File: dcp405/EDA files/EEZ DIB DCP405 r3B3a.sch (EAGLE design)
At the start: 317 parts, among them IC1 LM5145RGYT, IC10 TL072D, IC11 LTC2050HVCS8#PBF, IC12 SN74LVC1G3157DCKR, IC13 74AUP1G74DC.125, IC14 MCP23S17-E/SS, IC15 REF5025AIDR, IC16 TC77-5.0MCTTR, IC17 DAC8552IDGKR, IC18 SN74LVC1G3157DCKR, IC19 ADS1120IPWR, IC2 TPS54060DGQ, IC20 LM293D, IC21 MAX9141ESA, IC3 SI8641BB-B-IS1, IC4 SN74LVC1G139DCUR, IC5 MC78L05, IC6 MC79L05, IC7 SI8641BB-B-IS1, IC8 M24C32-WMN6P, IC9 TL072D, J1 4907, J2 FCR7350R, J3 FCR7350B, K1 FTR-C1GA005G-B05, Q1 BSC117N08NS5ATMA1, Q10 2N7002, Q11 BSS205NH6327XTSA1, Q12 PSMN0R9-25YLC, Q13 PSMN0R9-25YLC, Q14 BSS84P, Q15 BT139B-600E, Q16 2N7002, Q17 FMMT493TA, Q18 2N7002, Q19 PSMN013-60YL, Q2 BSC039N06NSATMA1, Q20 MMBT5551, Q21 2N7002, Q22 MMBT5401, Q23 MMBT5551, Q24 MMBT5551, Q25 2N7002, Q3 MMBT5401, Q4 D45H11FP, Q5 D45H11FP, Q6 FQPF11P06 or FQPF27P06, Q7 BCP56-16.115, Q8 MMBT5401, Q9 NZT605, X1 39-30-1020, X2 77317-104-20LF, X3 691322110005, X4 DS1024-2*10R0

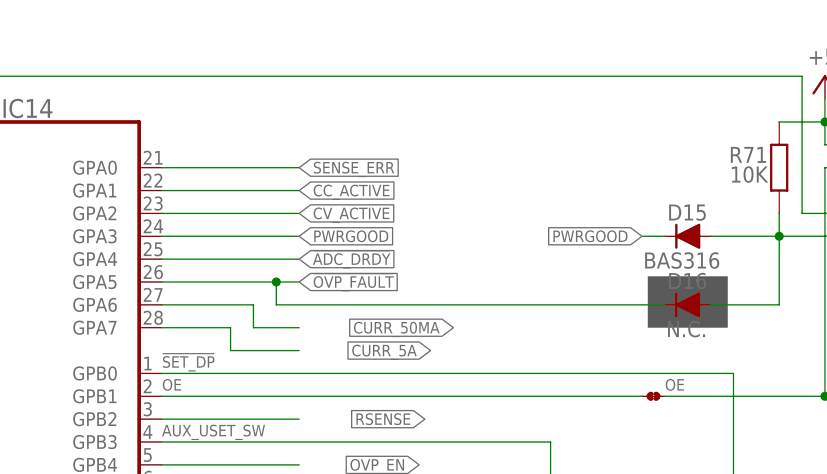
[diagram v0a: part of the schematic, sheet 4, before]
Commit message: Update Note 3.1. in DCP405 schematics
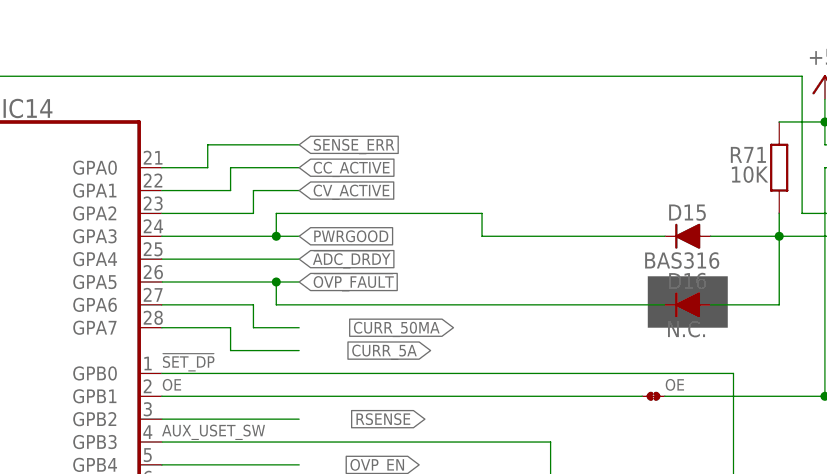
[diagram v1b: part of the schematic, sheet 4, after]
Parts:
- K1: device EEZ_Lib1:FTR-C1 -> EEZ_switches:FTR-C1
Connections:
- net N$115: now also K1-1.NO; no longer K1-1.O
- net N$116: now also K1-2.NO; no longer K1-2.O
- net POST_OUT+: now also K1-1.NC; no longer K1-1.S
- net POST_OUT-: now also K1-2.NC; no longer K1-2.S
- net SENSE+: now also K1-1.COM; no longer K1-1.P
- net SENSE-: now also K1-2.COM; no longer K1-2.P
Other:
- note added: "Note 3.1: Q4, Q5 and Q6 mounted on heatsink KK3"
- note removed: "Note 3.1: Q5, Q6 and Q7 mounted on heatsink KK3"
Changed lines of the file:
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@@
 <part name="C60" library="rcl" deviceset="C-EU" device="C0603" value="100n"/>
 <part name="P+14" library="supply2" deviceset="V+" device=""/>
-<part name="K1" library="EEZ_Lib1" deviceset="FTR-C1" device="" value="FTR-C1GA005G-B05"/>
+<part name="K1" library="EEZ_switches" deviceset="FTR-C1" device="" value="FTR-C1GA005G-B05"/>
 <part name="R3" library="rcl" deviceset="R-EU_" device="R0805" value="10K"/>
 <part name="D1" library="EEZ_Lib1" deviceset="DIODE" device="SOD323R" value="BAS316"/>
@@
 <wire x1="99.06" y1="119.38" x2="99.06" y2="73.66" width="0.1524" layer="97" style="shortdash"/>
 <wire x1="99.06" y1="73.66" x2="99.06" y2="58.42" width="0.1524" layer="97" style="shortdash"/>
-<text x="5.08" y="15.24" size="1.4224" layer="103">Note 3.1: Q5, Q6 and Q7 mounted on heatsink KK3</text>
+<text x="5.08" y="15.24" size="1.4224" layer="103">Note 3.1: Q4, Q5 and Q6 mounted on heatsink KK3</text>
 <wire x1="106.68" y1="173.99" x2="180.34" y2="173.99" width="0.1524" layer="97" style="shortdash"/>
 <wire x1="73.66" y1="58.42" x2="73.66" y2="17.78" width="0.1524" layer="97" style="shortdash"/>
@@
 <label x="86.36" y="154.94" size="1.27" layer="102" xref="yes"/>
 <pinref part="IC14" gate="A" pin="GPA3"/>
-<wire x1="71.12" y1="154.94" x2="86.36" y2="154.94" width="0.1524" layer="91"/>
-</segment>
-<segment>
+<wire x1="71.12" y1="154.94" x2="83.82" y2="154.94" width="0.1524" layer="91"/>
+<wire x1="83.82" y1="154.94" x2="86.36" y2="154.94" width="0.1524" layer="91"/>
+<wire x1="83.82" y1="154.94" x2="83.82" y2="157.48" width="0.1524" layer="91"/>
+<junction x="83.82" y="154.94"/>
 <pinref part="D15" gate="G$1" pin="C"/>
-<wire x1="127" y1="154.94" x2="124.46" y2="154.94" width="0.1524" layer="91"/>
-<label x="124.46" y="154.94" size="1.27" layer="102" rot="R180" xref="yes"/>
+<wire x1="127" y1="154.94" x2="106.68" y2="154.94" width="0.1524" layer="91"/>
+<wire x1="83.82" y1="157.48" x2="106.68" y2="157.48" width="0.1524" layer="91"/>
+<wire x1="106.68" y1="157.48" x2="106.68" y2="154.94" width="0.1524" layer="91"/>
 </segment>
 </net>
@@
 <net name="CV_ACTIVE" class="0">
 <segment>
-<label x="86.36" y="157.48" size="1.27" layer="102" xref="yes"/>
+<label x="86.36" y="160.02" size="1.27" layer="102" xref="yes"/>
 <pinref part="IC14" gate="A" pin="GPA2"/>
-<wire x1="71.12" y1="157.48" x2="86.36" y2="157.48" width="0.1524" layer="91"/>
+<wire x1="86.36" y1="160.02" x2="81.28" y2="160.02" width="0.1524" layer="91"/>
+<wire x1="81.28" y1="160.02" x2="81.28" y2="157.48" width="0.1524" layer="91"/>
+<wire x1="81.28" y1="157.48" x2="71.12" y2="157.48" width="0.1524" layer="91"/>
 </segment>
 </net>
 <net name="CC_ACTIVE" class="0">
 <segment>
-<label x="86.36" y="160.02" size="1.27" layer="102" xref="yes"/>
+<label x="86.36" y="162.56" size="1.27" layer="102" xref="yes"/>
 <pinref part="IC14" gate="A" pin="GPA1"/>
-<wire x1="71.12" y1="160.02" x2="86.36" y2="160.02" width="0.1524" layer="91"/>
+<wire x1="71.12" y1="160.02" x2="78.74" y2="160.02" width="0.1524" layer="91"/>
+<wire x1="78.74" y1="160.02" x2="78.74" y2="162.56" width="0.1524" layer="91"/>
+<wire x1="78.74" y1="162.56" x2="86.36" y2="162.56" width="0.1524" layer="91"/>
 </segment>
 </net>
@@
 <net name="SENSE_ERR" class="0">
 <segment>
-<label x="86.36" y="162.56" size="1.27" layer="102" xref="yes"/>
+<label x="86.36" y="165.1" size="1.27" layer="102" xref="yes"/>
 <pinref part="IC14" gate="A" pin="GPA0"/>
-<wire x1="71.12" y1="162.56" x2="86.36" y2="162.56" width="0.1524" layer="91"/>
+<wire x1="71.12" y1="162.56" x2="76.2" y2="162.56" width="0.1524" layer="91"/>
+<wire x1="76.2" y1="162.56" x2="76.2" y2="165.1" width="0.1524" layer="91"/>
+<wire x1="76.2" y1="165.1" x2="86.36" y2="165.1" width="0.1524" layer="91"/>
 </segment>
 </net>
@@
 <wire x1="162.56" y1="170.18" x2="152.4" y2="170.18" width="0.4064" layer="91"/>
 <label x="162.56" y="170.18" size="1.27" layer="102" rot="MR180" xref="yes"/>
-<pinref part="K1" gate="-1" pin="S"/>
+<pinref part="K1" gate="-1" pin="NC"/>
 <wire x1="152.4" y1="170.18" x2="149.86" y2="170.18" width="0.4064" layer="91"/>
 <wire x1="111.76" y1="160.02" x2="114.3" y2="160.02" width="0.1524" layer="91"/>
@@
 <wire x1="96.52" y1="157.48" x2="96.52" y2="139.7" width="0.1524" layer="91"/>
 <junction x="96.52" y="139.7"/>
-<pinref part="K1" gate="-1" pin="P"/>
+<pinref part="K1" gate="-1" pin="COM"/>
 <wire x1="96.52" y1="157.48" x2="104.14" y2="157.48" width="0.1524" layer="91"/>
 </segment>
@@
 <junction x="96.52" y="124.46"/>
 <wire x1="71.12" y1="124.46" x2="96.52" y2="124.46" width="0.1524" layer="91"/>
-<pinref part="K1" gate="-2" pin="P"/>
+<pinref part="K1" gate="-2" pin="COM"/>
 <wire x1="104.14" y1="106.68" x2="96.52" y2="106.68" width="0.1524" layer="91"/>
 </segment>
@@
 <wire x1="114.3" y1="104.14" x2="114.3" y2="99.06" width="0.1524" layer="91"/>
 <junction x="114.3" y="99.06"/>
-<pinref part="K1" gate="-2" pin="S"/>
+<pinref part="K1" gate="-2" pin="NC"/>
 <wire x1="111.76" y1="104.14" x2="114.3" y2="104.14" width="0.1524" layer="91"/>
 <wire x1="162.56" y1="119.38" x2="157.48" y2="119.38" width="0.4064" layer="91"/>
@@
 <wire x1="203.2" y1="152.4" x2="114.3" y2="152.4" width="0.1524" layer="91"/>
 <pinref part="X3" gate="-4" pin="1"/>
-<pinref part="K1" gate="-1" pin="O"/>
+<pinref part="K1" gate="-1" pin="NO"/>
 <wire x1="111.76" y1="154.94" x2="114.3" y2="154.94" width="0.1524" layer="91"/>
 <wire x1="114.3" y1="154.94" x2="114.3" y2="152.4" width="0.1524" layer="91"/>
@@
 <pinref part="X3" gate="-5" pin="1"/>
 <wire x1="114.3" y1="109.22" x2="114.3" y2="111.76" width="0.1524" layer="91"/>
-<pinref part="K1" gate="-2" pin="O"/>
+<pinref part="K1" gate="-2" pin="NO"/>
 <wire x1="111.76" y1="109.22" x2="114.3" y2="109.22" width="0.1524" layer="91"/>
 </segment>
